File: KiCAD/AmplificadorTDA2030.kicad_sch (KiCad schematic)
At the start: 39 parts, among them J1 R_Speaker, J2 SJ1-3523N, J3 DC-005, J4 L_Speaker, U1 TDA2030, U2 TDA2030

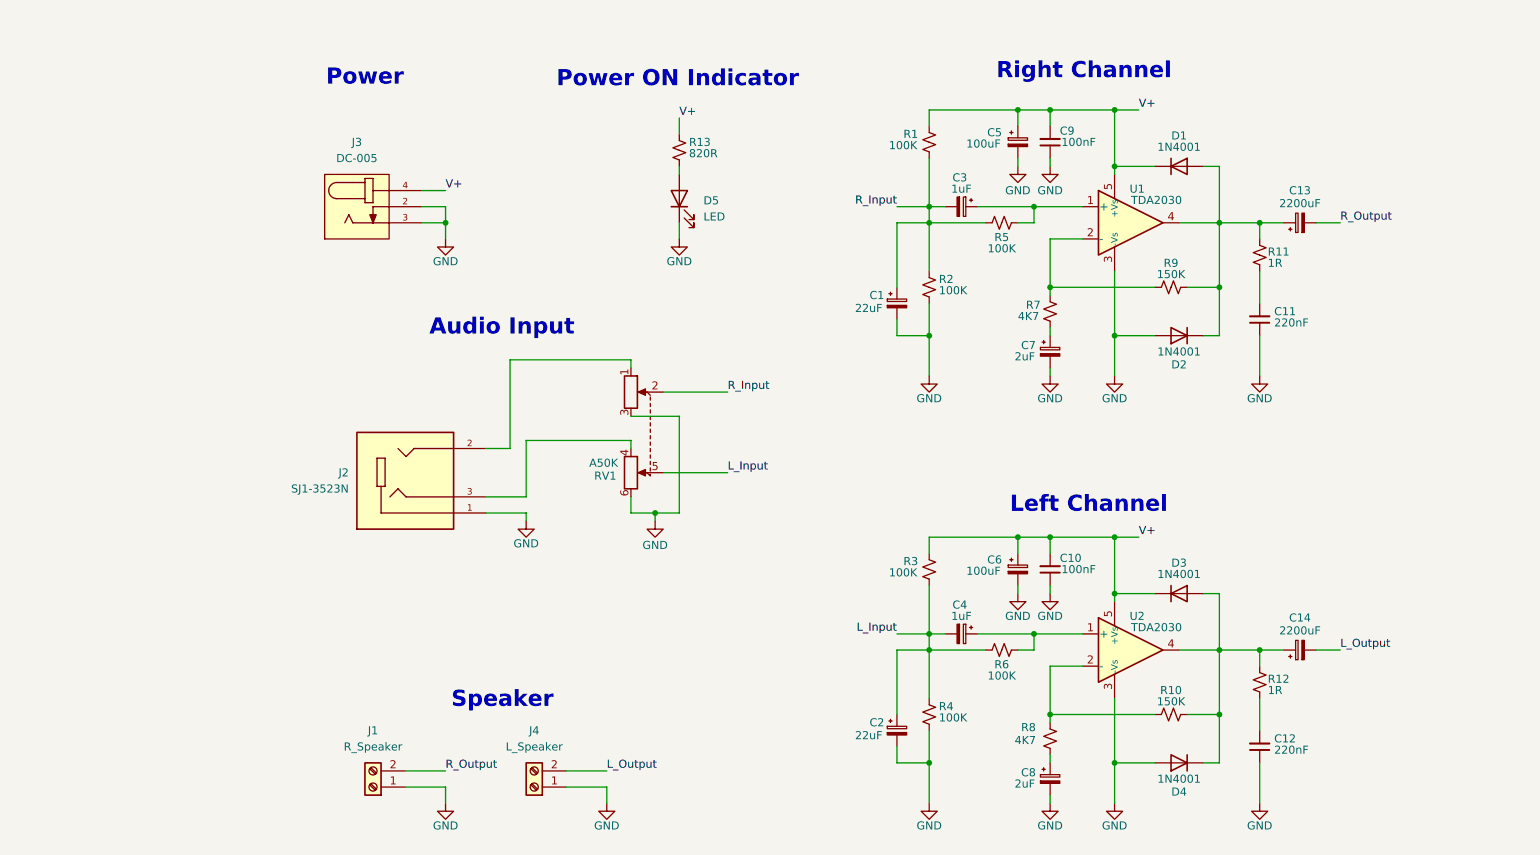
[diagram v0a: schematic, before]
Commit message: Reorganizacion de Carpetas y Actualizacion de Documentacion
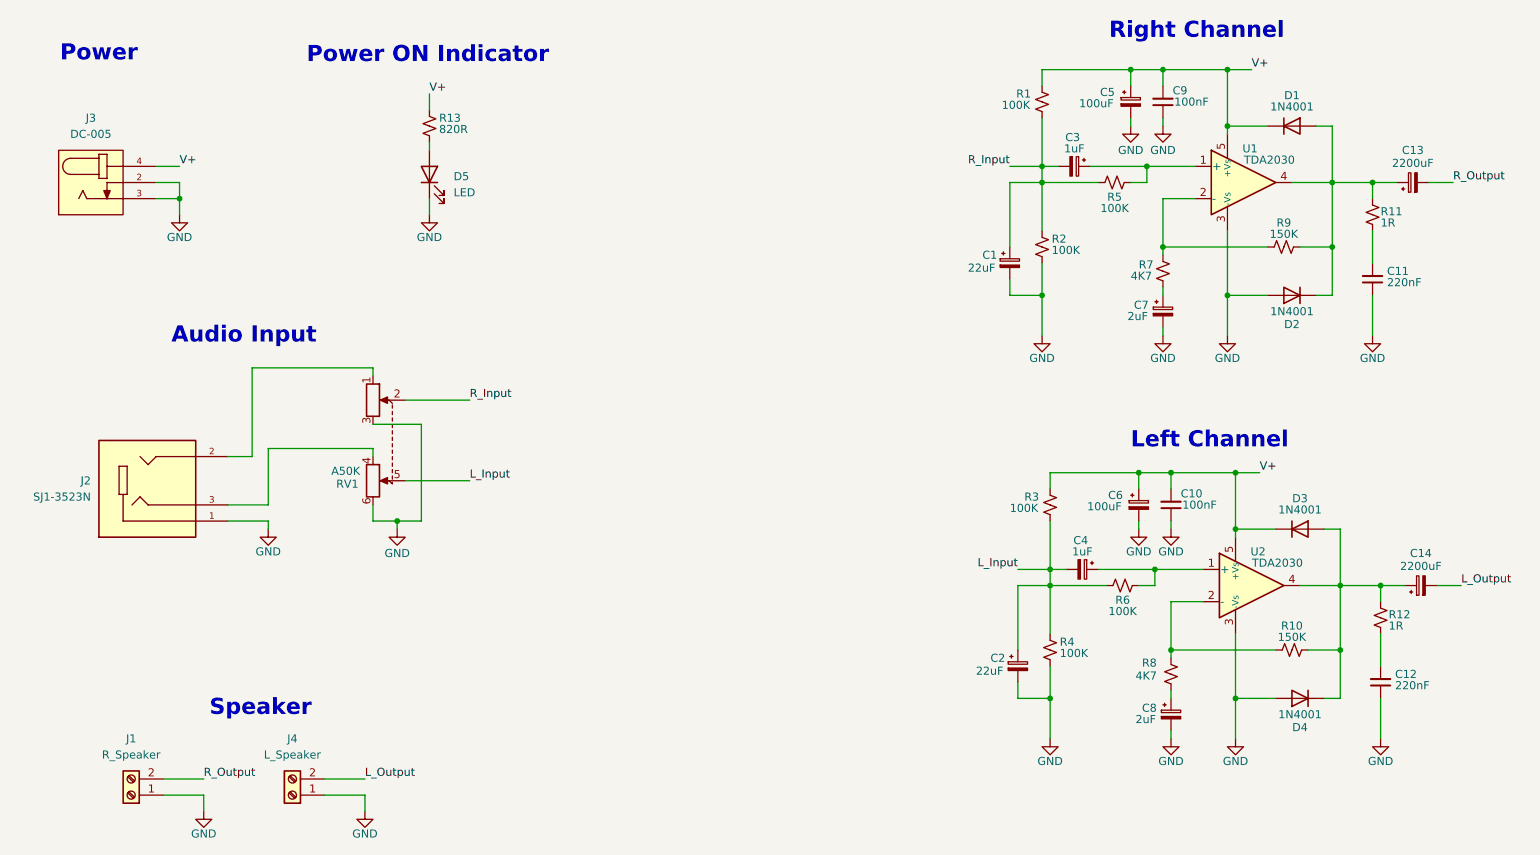
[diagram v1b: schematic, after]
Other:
- moved on the sheet: C1, C10, C11, C12, C13, C14, C2, C3, C4, C5, C6, C7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

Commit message: Archivos Imprimibles
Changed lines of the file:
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@@
 (kicad_sch
-	(version 20231120)
+	(version 20250114)
 	(generator "eeschema")
-	(generator_version "8.0")
+	(generator_version "9.0")
 	(paper "A4")
 	(title_block
@@
 		(company "Decima Enrique Emanuel")
 	)
+	(text "Right Channel"
+		(exclude_from_sim no)
+		(at 207.264 16.764 0)
+		(effects
+			(font
+				(face "KiCad Font")
+				(size 2.54 2.54)
+				(thickness 0.508)
+				(bold yes)
+			)
+		)
+	)
+	(text "Power ON Indicator"
+		(exclude_from_sim no)
+		(at 86.106 20.574 0)
+		(effects
+			(font
+				(face "KiCad Font")
+				(size 2.54 2.54)
+				(thickness 0.508)
+				(bold yes)
+			)
+		)
+	)
+	(text "Power"
+		(exclude_from_sim no)
+		(at 34.29 20.32 0)
+		(effects
+			(font
+				(face "KiCad Font")
+				(size 2.54 2.54)
+				(thickness 0.508)
+				(bold yes)
+			)
+		)
+	)
+	(text "Speaker"
+		(exclude_from_sim no)
+		(at 67.818 123.444 0)
+		(effects
+			(font
+				(face "KiCad Font")
+				(size 2.54 2.54)
+				(thickness 0.508)
+				(bold yes)
+			)
+			(justify right)
+		)
+	)
+	(text "Left Channel"
+		(exclude_from_sim no)
+		(at 209.296 81.28 0)
+		(effects
+			(font
+				(face "KiCad Font")
+				(size 2.54 2.54)
+				(thickness 0.508)
+				(bold yes)
+			)
+		)
+	)
+	(text "Audio Input"
+		(exclude_from_sim no)
+		(at 57.15 64.77 0)
+		(effects
+			(font
+				(face "KiCad Font")
+				(size 2.54 2.54)
+				(thickness 0.508)
+				(bold yes)
+			)
+		)
+	)
 	(junction
 		(at 228.6 50.8)
@@
 		)
 	)
-	(text "Right Channel"
-		(exclude_from_sim no)
-		(at 207.264 16.764 0)
-		(effects
-			(font
-				(face "KiCad Font")
-				(size 2.54 2.54)
-				(thickness 0.508)
-				(bold yes)
-			)
-		)
-	)
-	(text "Power ON Indicator"
-		(exclude_from_sim no)
-		(at 86.106 20.574 0)
-		(effects
-			(font
-				(face "KiCad Font")
-				(size 2.54 2.54)
-				(thickness 0.508)
-				(bold yes)
-			)
-		)
-	)
-	(text "Power"
-		(exclude_from_sim no)
-		(at 34.29 20.32 0)
-		(effects
-			(font
-				(face "KiCad Font")
-				(size 2.54 2.54)
-				(thickness 0.508)
-				(bold yes)
-			)
-		)
-	)
-	(text "Speaker"
-		(exclude_from_sim no)
-		(at 67.818 123.444 0)
-		(effects
-			(font
-				(face "KiCad Font")
-				(size 2.54 2.54)
-				(thickness 0.508)
-				(bold yes)
-			)
-			(justify right)
-		)
-	)
-	(text "Left Channel"
-		(exclude_from_sim no)
-		(at 209.296 81.28 0)
-		(effects
-			(font
-				(face "KiCad Font")
-				(size 2.54 2.54)
-				(thickness 0.508)
-				(bold yes)
-			)
-		)
-	)
-	(text "Audio Input"
-		(exclude_from_sim no)
-		(at 57.15 64.77 0)
-		(effects
-			(font
-				(face "KiCad Font")
-				(size 2.54 2.54)
-				(thickness 0.508)
-				(bold yes)
-			)
-		)
-	)
 	(label "R_Output"
 		(at 50.8 134.62 0)
-		(fields_autoplaced yes)
 		(effects
 			(font
@@
 	(label "V+"
 		(at 86.36 26.67 0)
-		(fields_autoplaced yes)
 		(effects
 			(font
@@
 	(label "L_Input"
 		(at 92.71 87.63 0)
-		(fields_autoplaced yes)
 		(effects
 			(font
@@
 	(label "V+"
 		(at 46.99 38.1 0)
-		(fields_autoplaced yes)
 		(effects
 			(font
@@
 	(label "R_Input"
 		(at 177.8 38.1 180)
-		(fields_autoplaced yes)
 		(effects
 			(font
@@
 	(label "R_Output"
 		(at 247.65 40.64 0)
-		(fields_autoplaced yes)
 		(effects
 			(font
@@
 	(label "L_Output"
 		(at 76.2 134.62 0)
-		(fields_autoplaced yes)
 		(effects
 			(font
@@
 	(label "L_Input"
 		(at 179.07 101.6 180)
-		(fields_autoplaced yes)
 		(effects
 			(font
@@
 	(label "V+"
 		(at 217.17 86.36 0)
-		(fields_autoplaced yes)
 		(effects
 			(font
@@
 	(label "L_Output"
 		(at 248.92 104.14 0)
-		(fields_autoplaced yes)
 		(effects
 			(font
@@
 	(label "R_Input"
 		(at 92.71 74.93 0)
-		(fields_autoplaced yes)
 		(effects
 			(font
@@
 	(label "V+"
 		(at 215.9 22.86 0)
-		(fields_autoplaced yes)
 		(effects
 			(font
@@
 		)
 	)
+	(embedded_fonts no)
 )
